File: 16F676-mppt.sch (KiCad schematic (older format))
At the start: 47 parts, among them J1 S+, J2 S-, J3 VB+, J4 VB-, Q1 BUK9511-55A127, Q2 BUK9511-55A127, Q3 2N2222A, Q4 2N2222A, Q5 2N2907A, SW1 Write OP-AMP DIFF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

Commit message: add note for R15.
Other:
- note added: "R15\n6A = 2.2k, 3A = 4.7k"
- note added: "x20(6A)"
- note removed: "x47(50, 6A)"
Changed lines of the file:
@@
 Connection ~ 9200 4850
 Text Notes 9100 3850 0    60   ~ 0
-x47(50, 6A)
+x20(6A)
 Wire Wire Line
 	2300 4100 2750 4100
@@
 Wire Wire Line
 	4100 5600 5900 5600
+Text Notes 10100 4300 0    60   ~ 0
+R15\n6A = 2.2k, 3A = 4.7k
 $EndSCHEMATC

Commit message: add clamp.
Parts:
- added Q6, Q7: 2N2222A, TO_SOT_Packages_THT:TO-92_Inline_Wide, symbol Device:Q_NPN_EBC
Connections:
- net GND: now also Q7.1 (E)
- net PV-Voltage: now also Q6.1 (E)
- new net: Q6.2 (B), Q6.3 (C), Q7.2 (B), Q7.3 (C)
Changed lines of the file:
@@
 Sheet 1 1
 Title "Simple MPPT with 16F676 v1"
-Date "2018-12-17"
-Rev "1.6"
+Date "2018-12-26"
+Rev "1.8"
 Comp ""
 Comment1 ""
@@
 Wire Wire Line
 	5450 3600 6350 3600
-Wire Wire Line
-	1500 4200 1500 5600
 Connection ~ 1500 5600
 Wire Wire Line
@@
 	1900 2200 2400 2200
 Wire Wire Line
-	2300 5600 1500 5600
+	2300 5600 1750 5600
 Wire Wire Line
 	1500 2200 1900 2200
@@
 Text Notes 10100 4300 0    60   ~ 0
 R15\n6A = 2.2k, 3A = 4.7k
+$Comp
+L Device:Q_NPN_EBC Q6
+U 1 1 5C242C61
+P 1850 4800
+F 0 "Q6" H 2150 4700 50  0000 R CNN
+F 1 "2N2222A" H 2350 4850 50  0000 R CNN
+F 2 "TO_SOT_Packages_THT:TO-92_Inline_Wide" H 2050 4900 29  0001 C CNN
+F 3 "" H 1850 4800 60  0000 C CNN
+	1    1850 4800
+	-1   0    0    1
+$EndComp
+$Comp
+L Device:Q_NPN_EBC Q7
+U 1 1 5C242D25
+P 1850 5300
+F 0 "Q7" H 2150 5200 50  0000 R CNN
+F 1 "2N2222A" H 2350 5350 50  0000 R CNN
+F 2 "TO_SOT_Packages_THT:TO-92_Inline_Wide" H 2050 5400 29  0001 C CNN
+F 3 "" H 1850 5300 60  0000 C CNN
+	1    1850 5300
+	-1   0    0    -1
+$EndComp
+Wire Wire Line
+	1500 4200 1500 5600
+Wire Wire Line
+	1750 5000 1750 5050
+Wire Wire Line
+	1750 4400 1750 4600
+Connection ~ 1750 4400
+Wire Wire Line
+	2050 4800 2050 5050
+Wire Wire Line
+	2050 5050 1750 5050
+Connection ~ 2050 5050
+Wire Wire Line
+	2050 5050 2050 5300
+Connection ~ 1750 5050
+Wire Wire Line
+	1750 5050 1750 5100
+Wire Wire Line
+	1750 5500 1750 5600
+Connection ~ 1750 5600
+Wire Wire Line
+	1750 5600 1500 5600
 $EndSCHEMATC

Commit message: Fix High-z turn on FET problem.
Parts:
- added R11: 10k, Resistors_THT:R_Axial_DIN0309_L9.0mm_D3.2mm_P12.70mm_Horizontal, symbol Device:R
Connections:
- net BootStrap: now also R11.1
- net at R7.2, U3.9 (RC1/AN5): now also R11.2
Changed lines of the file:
@@
 Sheet 1 1
 Title "Simple MPPT with 16F676 v1"
-Date "2018-12-26"
-Rev "1.8"
+Date "2019-02-13"
+Rev "1.81"
 Comp ""
 Comment1 ""
@@
 Connection ~ 6100 2350
 Wire Wire Line
-	3150 2350 5450 2350
+	3150 2350 5350 2350
 Wire Wire Line
 	6500 2700 6550 2700
@@
 Wire Wire Line
 	1750 5600 1500 5600
+$Comp
+L Device:R R11
+U 1 1 5C644B4D
+P 5350 2750
+F 0 "R11" V 5430 2750 50  0000 C CNN
+F 1 "10k" V 5350 2750 50  0000 C CNN
+F 2 "Resistors_THT:R_Axial_DIN0309_L9.0mm_D3.2mm_P12.70mm_Horizontal" V 5280 2750 30  0001 C CNN
+F 3 "" H 5350 2750 30  0000 C CNN
+	1    5350 2750
+	1    0    0    -1
+$EndComp
+Wire Wire Line
+	5350 2900 5350 3100
+Wire Wire Line
+	5350 3100 5550 3100
+Wire Wire Line
+	5550 3100 5550 3400
+Connection ~ 5550 3400
+Wire Wire Line
+	5350 2600 5350 2350
+Connection ~ 5350 2350
+Wire Wire Line
+	5350 2350 5450 2350
 $EndSCHEMATC

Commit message: Fix R1, R15 values.
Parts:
- R1: value 2.2k -> 10k
- R15: value 2.2k -> 3.3k
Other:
- note added: "R15 3A = 4.7k"
- note removed: "R15\n6A = 2.2k, 3A = 4.7k"
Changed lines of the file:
@@
 Sheet 1 1
 Title "Simple MPPT with 16F676 v1"
-Date "2019-02-13"
-Rev "1.81"
+Date "2019-02-15"
+Rev "1.82"
 Comp ""
 Comment1 ""
@@
 P 9450 4850
 F 0 "R1" V 9530 4850 50  0000 C CNN
-F 1 "2.2k" V 9450 4850 50  0000 C CNN
+F 1 "10k" V 9450 4850 50  0000 C CNN
 F 2 "Resistors_THT:R_Axial_DIN0309_L9.0mm_D3.2mm_P12.70mm_Horizontal" V 9380 4850 50  0001 C CNN
 F 3 "" H 9450 4850 50  0000 C CNN
@@
 P 9900 4300
 F 0 "R15" V 9980 4300 50  0000 C CNN
-F 1 "2.2k" V 9900 4300 50  0000 C CNN
+F 1 "3.3k" V 9900 4300 50  0000 C CNN
 F 2 "Resistors_THT:R_Axial_DIN0309_L9.0mm_D3.2mm_P12.70mm_Horizontal" V 9830 4300 50  0001 C CNN
 F 3 "" H 9900 4300 50  0000 C CNN
@@
 	4100 5600 5900 5600
 Text Notes 10100 4300 0    60   ~ 0
-R15\n6A = 2.2k, 3A = 4.7k
+R15 3A = 4.7k
 $Comp
 L Device:Q_NPN_EBC Q6

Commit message: Update current sensing resistors.
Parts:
- R2, R4: value 100k -> 47k
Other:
- note added: "13.3(6A)"
- note added: "3A, R2 = R4 = 100k"
- note removed: "R15 3A = 4.7k"
- note removed: "x20(6A)"
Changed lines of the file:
@@
 P 7300 4250
 F 0 "R4" V 7380 4250 50  0000 C CNN
-F 1 "100k" V 7300 4250 50  0000 C CNN
+F 1 "47k" V 7300 4250 50  0000 C CNN
 F 2 "Resistors_THT:R_Axial_DIN0309_L9.0mm_D3.2mm_P12.70mm_Horizontal" V 7230 4250 30  0001 C CNN
 F 3 "" H 7300 4250 30  0000 C CNN
@@
 P 6950 5300
 F 0 "R2" V 7030 5300 50  0000 C CNN
-F 1 "100k" V 6950 5300 50  0000 C CNN
+F 1 "47k" V 6950 5300 50  0000 C CNN
 F 2 "Resistors_THT:R_Axial_DIN0309_L9.0mm_D3.2mm_P12.70mm_Horizontal" V 6880 5300 30  0001 C CNN
 F 3 "" H 6950 5300 30  0000 C CNN
@@
 Connection ~ 9200 4850
 Text Notes 9100 3850 0    60   ~ 0
-x20(6A)
+13.3(6A)
 Wire Wire Line
 	2300 4100 2750 4100
@@
 	4100 5600 5900 5600
 Text Notes 10100 4300 0    60   ~ 0
-R15 3A = 4.7k
+3A, R2 = R4 = 100k
 $Comp
 L Device:Q_NPN_EBC Q6

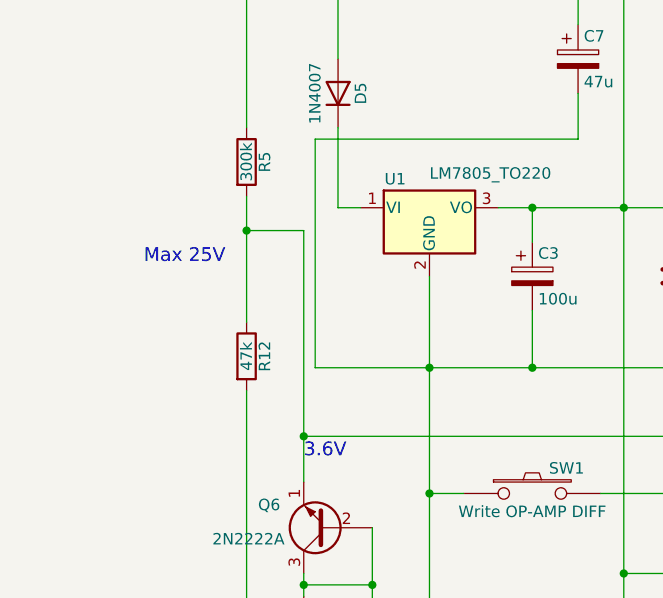
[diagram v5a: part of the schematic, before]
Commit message: Add hint for 48V input.
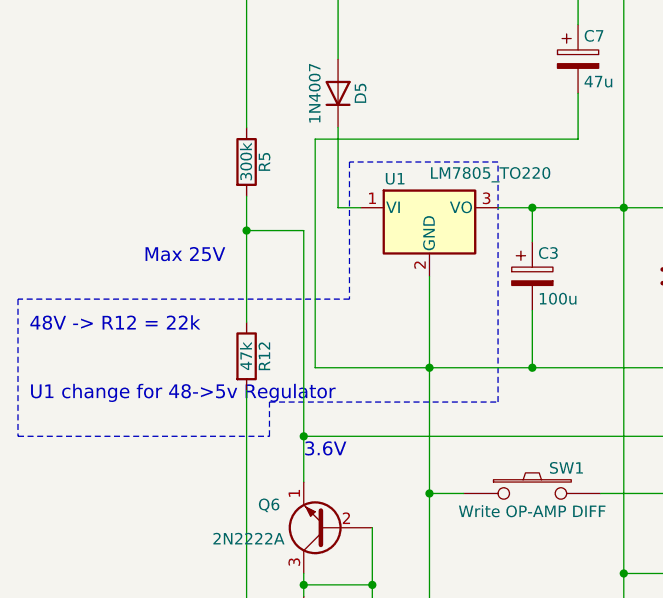
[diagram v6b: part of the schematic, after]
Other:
- note added: "48V -> R12 = 22k"
- note added: "U1 change for 48->5v Regulator"
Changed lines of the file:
@@
 Wire Wire Line
 	5350 2350 5450 2350
+Text Notes 550  3950 0    60   ~ 0
+48V -> R12 = 22k
+Wire Notes Line
+	500  3800 500  4400
+Wire Notes Line
+	500  4400 1600 4400
+Wire Notes Line
+	1600 4400 1600 4250
+Wire Notes Line
+	1600 4250 2600 4250
+Wire Notes Line
+	2600 4250 2600 3200
+Wire Notes Line
+	2600 3200 1950 3200
+Wire Notes Line
+	1950 3200 1950 3800
+Wire Notes Line
+	1950 3800 500  3800
+Text Notes 550  4250 0    60   ~ 0
+U1 change for 48->5v Regulator
 $EndSCHEMATC

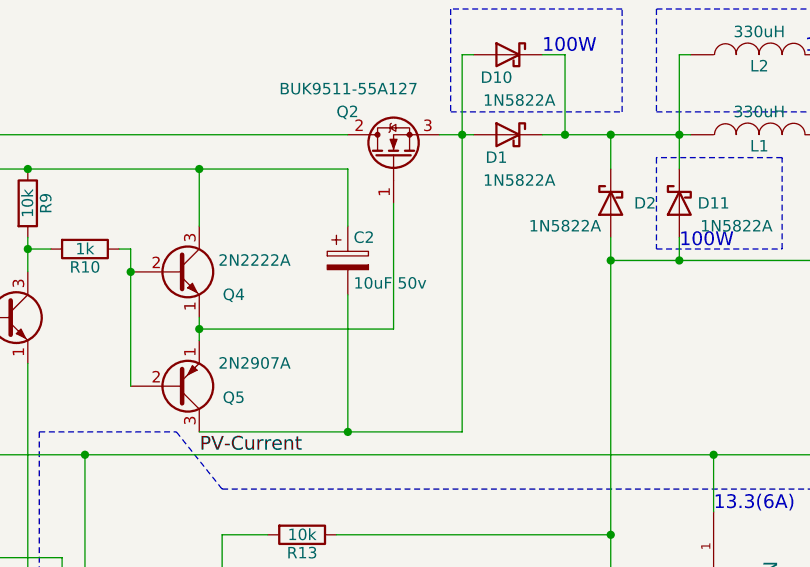
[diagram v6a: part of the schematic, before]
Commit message: C2 -> 4.7uF
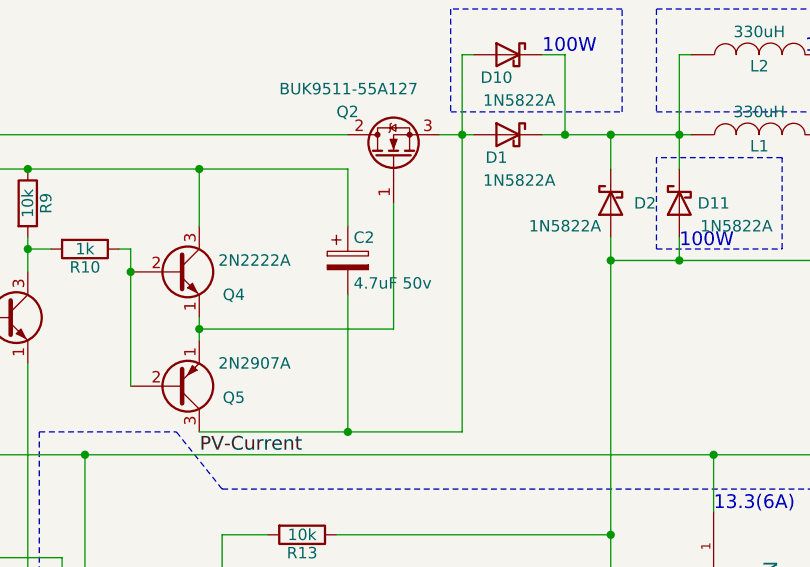
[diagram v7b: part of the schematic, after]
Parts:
- C2: value 10uF 50v -> 4.7uF 50v
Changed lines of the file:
@@
 EESchema Schematic File Version 4
-LIBS:16F676-mppt-cache
-EELAYER 26 0
+EELAYER 30 0
 EELAYER END
 $Descr A4 11693 8268
@@
 P 7500 2750
 F 0 "C2" H 7525 2850 50  0000 L CNN
-F 1 "10uF 50v" H 7525 2650 50  0000 L CNN
+F 1 "4.7uF 50v" H 7525 2650 50  0000 L CNN
 F 2 "Capacitors_THT:CP_Radial_D12.5mm_P5.00mm" H 7538 2600 30  0001 C CNN
 F 3 "" H 7500 2750 60  0000 C CNN

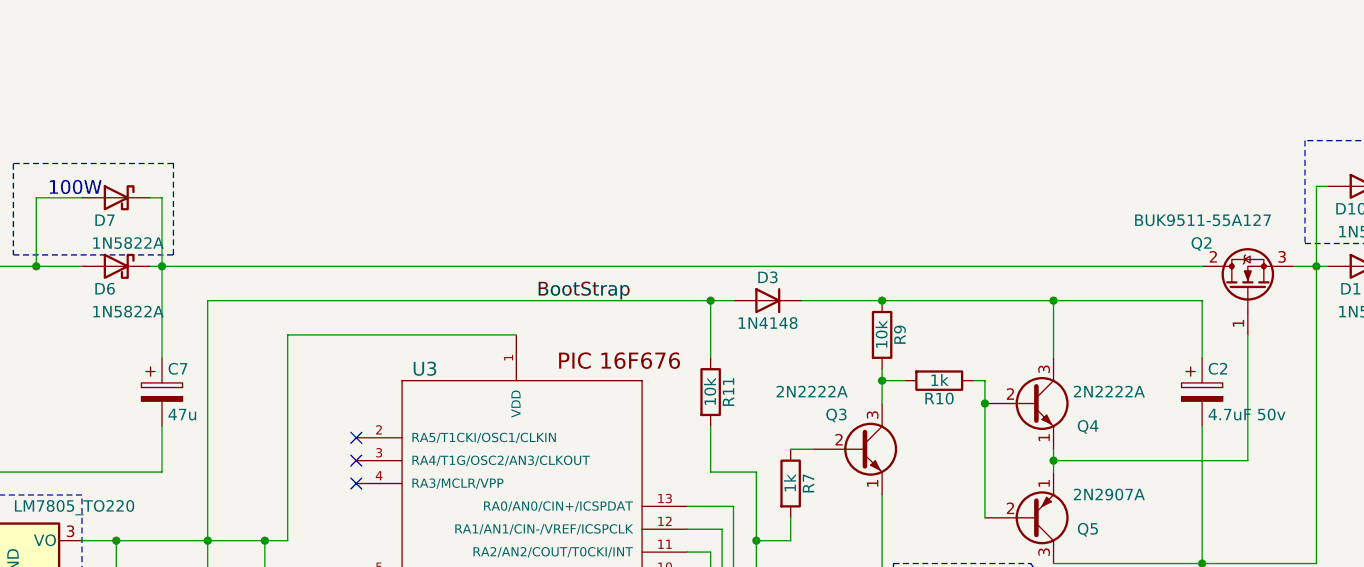
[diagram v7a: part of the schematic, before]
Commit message: Fix Bootstrap problem.
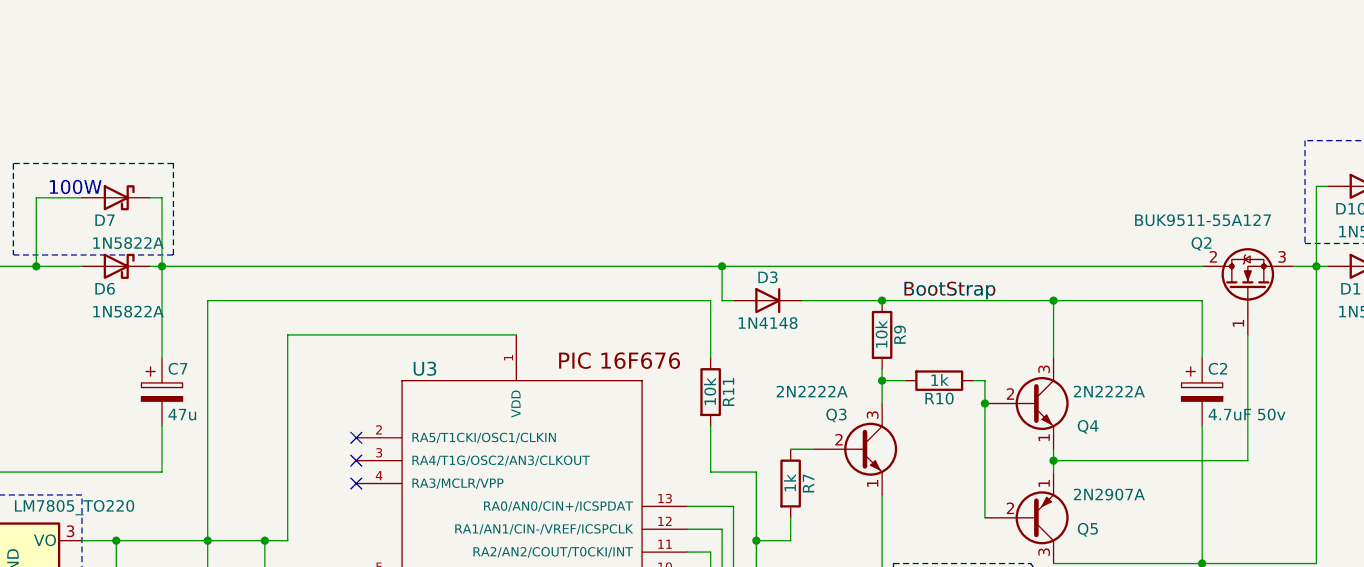
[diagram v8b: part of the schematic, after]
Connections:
- net BootStrap: now also C2.1, D3.1 (K), Q4.3 (C), R9.1; no longer C3.1, C4.1, D3.2 (A), R11.1, R14.1, R16.2, U1.3 (VO), U2.8 (V+), U2.8 (V+), U3.1 (VDD)
- net at C7.1, D6.1 (K), D7.1 (K)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: now also D3.2 (A)
- new net: C3.1, C4.1, R11.1, R14.1, R16.2, U1.3 (VO), U2.8 (V+), U2.8 (V+), U3.1 (VDD)
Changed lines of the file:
@@
 	1    0    0    -1
 $EndComp
-Text Label 5000 2350 2    60   ~ 0
+Text Label 6600 2350 2    60   ~ 0
 BootStrap
 Text Label 7300 3600 2    60   ~ 0
@@
 	9100 3600 9900 3600
 Wire Wire Line
-	2950 2200 7500 2200
+	2950 2200 5400 2200
 Wire Wire Line
 	2950 2200 2950 2600
@@
 Wire Wire Line
 	5350 2600 5350 2350
-Connection ~ 5350 2350
-Wire Wire Line
-	5350 2350 5450 2350
 Text Notes 550  3950 0    60   ~ 0
 48V -> R12 = 22k
@@
 Text Notes 550  4250 0    60   ~ 0
 U1 change for 48->5v Regulator
+Wire Wire Line
+	5450 2350 5400 2350
+Wire Wire Line
+	5400 2350 5400 2200
+Connection ~ 5400 2200
+Wire Wire Line
+	5400 2200 7500 2200
 $EndSCHEMATC
